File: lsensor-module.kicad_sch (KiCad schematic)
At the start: 27 parts, among them CN4 XHP-2, CN5 B2B-XH-A, Q4 BC847, U6 LMV358ID

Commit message: Назначение посадочных мест схемы
Дорисовка недостающий э/компонентов и важных 3D-моделей
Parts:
- R19: footprint lib:TRIM_PTN10-A01HB20 -> lib:Potentiometer_Bochen_PT10
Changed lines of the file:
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@@
 			)
 		)
-		(property "Footprint" "lib:TRIM_PTN10-A01HB20"
+		(property "Footprint" "lib:Potentiometer_Bochen_PT10"
 			(at 73.66 77.47 0)
 			(effects

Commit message: Разводка ПП, трассировка, оптимизация
Отказ от идеи с субмодулем, все разводится на двухсторонней ПП.
Вынос аналогового фотореле на отдельный лист схемы.
Разводка двусторонней ПП
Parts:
- R19: footprint lib:Potentiometer_Bochen_PT10 -> lib:TRIM_PTN10-A01HB20; Part Number PTN10-A200SB20 -> PTN10-A200HB20
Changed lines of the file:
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@@
 			)
 		)
-		(property "Footprint" "lib:Potentiometer_Bochen_PT10"
+		(property "Footprint" "lib:TRIM_PTN10-A01HB20"
 			(at 73.66 77.47 0)
 			(effects
@@
 			)
 		)
-		(property "Part Number" " PTN10-A200SB20"
+		(property "Part Number" "PTN10-A200HB20"
 			(at 76.962 88.392 90)
 			(effects

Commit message: Доделка ПП до финала
Проверка DRC, подгонка автоправил трассирования дорожек. Корректировка технических ограничений ПП. Расчет номиналов конденсаторов C11, C12.
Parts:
- renumbered C16 to C14, C17 to C15, C18 to C16, C19 to C17, C20 to C18, C21 to C19, C22 to C20, C23 to C21
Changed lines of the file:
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@@
 		(on_board yes)
 		(dnp no)
-		(property "Reference" "C22"
+		(property "Reference" "C20"
 			(at 162.56 76.2 0)
 			(effects
@@
 			(project "Camping-LightRelay"
 				(path "/5869d0d8-0214-47f7-a5b8-c2b5f6821b5d/65ad4b19-8f8d-472a-8529-1f5862972991"
-					(reference "C22")
+					(reference "C20")
 					(unit 1)
 				)
@@
 		(dnp no)
 		(fields_autoplaced yes)
-		(property "Reference" "#PWR028"
+		(property "Reference" "#PWR027"
 			(at 162.56 116.84 0)
 			(effects
@@
 			(project "Camping-LightRelay"
 				(path "/5869d0d8-0214-47f7-a5b8-c2b5f6821b5d/65ad4b19-8f8d-472a-8529-1f5862972991"
-					(reference "#PWR028")
+					(reference "#PWR027")
 					(unit 1)
 				)
@@
 		(on_board yes)
 		(dnp no)
-		(property "Reference" "C18"
+		(property "Reference" "C16"
 			(at 116.332 56.134 90)
 			(effects
@@
 			(project "Camping-LightRelay"
 				(path "/5869d0d8-0214-47f7-a5b8-c2b5f6821b5d/65ad4b19-8f8d-472a-8529-1f5862972991"
-					(reference "C18")
+					(reference "C16")
 					(unit 1)
 				)
@@
 		(dnp no)
 		(fields_autoplaced yes)
-		(property "Reference" "#PWR021"
+		(property "Reference" "#PWR020"
 			(at 73.66 116.84 0)
 			(effects
@@
 			(project "Camping-LightRelay"
 				(path "/5869d0d8-0214-47f7-a5b8-c2b5f6821b5d/65ad4b19-8f8d-472a-8529-1f5862972991"
-					(reference "#PWR021")
+					(reference "#PWR020")
 					(unit 1)
 				)
@@
 		(dnp no)
 		(fields_autoplaced yes)
-		(property "Reference" "#PWR025"
+		(property "Reference" "#PWR024"
 			(at 109.22 116.84 0)
 			(effects
@@
 			(project "Camping-LightRelay"
 				(path "/5869d0d8-0214-47f7-a5b8-c2b5f6821b5d/65ad4b19-8f8d-472a-8529-1f5862972991"
-					(reference "#PWR025")
+					(reference "#PWR024")
 					(unit 1)
 				)
@@
 		(on_board yes)
 		(dnp no)
-		(property "Reference" "C21"
+		(property "Reference" "C19"
 			(at 152.146 87.63 0)
 			(effects
@@
 			(project "Camping-LightRelay"
 				(path "/5869d0d8-0214-47f7-a5b8-c2b5f6821b5d/65ad4b19-8f8d-472a-8529-1f5862972991"
-					(reference "C21")
+					(reference "C19")
 					(unit 1)
 				)
@@
 		(dnp no)
 		(fields_autoplaced yes)
-		(property "Reference" "#PWR029"
+		(property "Reference" "#PWR028"
 			(at 170.18 116.84 0)
 			(effects
@@
 			(project "Camping-LightRelay"
 				(path "/5869d0d8-0214-47f7-a5b8-c2b5f6821b5d/65ad4b19-8f8d-472a-8529-1f5862972991"
-					(reference "#PWR029")
+					(reference "#PWR028")
 					(unit 1)
 				)
@@
 		(on_board yes)
 		(dnp no)
-		(property "Reference" "C19"
+		(property "Reference" "C17"
 			(at 130.81 65.278 0)
 			(effects
@@
 			(project "Camping-LightRelay"
 				(path "/5869d0d8-0214-47f7-a5b8-c2b5f6821b5d/65ad4b19-8f8d-472a-8529-1f5862972991"
-					(reference "C19")
+					(reference "C17")
 					(unit 1)
 				)
@@
 		(on_board yes)
 		(dnp no)
-		(property "Reference" "C16"
+		(property "Reference" "C14"
 			(at 90.17 70.866 0)
 			(effects
@@
 			(project "Camping-LightRelay"
 				(path "/5869d0d8-0214-47f7-a5b8-c2b5f6821b5d/65ad4b19-8f8d-472a-8529-1f5862972991"
-					(reference "C16")
+					(reference "C14")
 					(unit 1)
 				)
@@
 		(on_board yes)
 		(dnp no)
-		(property "Reference" "C23"
+		(property "Reference" "C21"
 			(at 191.77 90.678 90)
 			(effects
@@
 			(project "Camping-LightRelay"
 				(path "/5869d0d8-0214-47f7-a5b8-c2b5f6821b5d/65ad4b19-8f8d-472a-8529-1f5862972991"
-					(reference "C23")
+					(reference "C21")
 					(unit 1)
 				)
@@
 		(dnp no)
 		(fields_autoplaced yes)
-		(property "Reference" "#PWR023"
+		(property "Reference" "#PWR022"
 			(at 96.52 116.84 0)
 			(effects
@@
 			(project "Camping-LightRelay"
 				(path "/5869d0d8-0214-47f7-a5b8-c2b5f6821b5d/65ad4b19-8f8d-472a-8529-1f5862972991"
-					(reference "#PWR023")
+					(reference "#PWR022")
 					(unit 1)
 				)
@@
 		(dnp no)
 		(fields_autoplaced yes)
-		(property "Reference" "#PWR026"
+		(property "Reference" "#PWR025"
 			(at 138.43 116.84 0)
 			(effects
@@
 			(project "Camping-LightRelay"
 				(path "/5869d0d8-0214-47f7-a5b8-c2b5f6821b5d/65ad4b19-8f8d-472a-8529-1f5862972991"
-					(reference "#PWR026")
+					(reference "#PWR025")
 					(unit 1)
 				)
@@
 		(dnp no)
 		(fields_autoplaced yes)
-		(property "Reference" "#PWR031"
+		(property "Reference" "#PWR030"
 			(at 209.55 69.85 0)
 			(effects
@@
 			(project "Camping-LightRelay"
 				(path "/5869d0d8-0214-47f7-a5b8-c2b5f6821b5d/65ad4b19-8f8d-472a-8529-1f5862972991"
-					(reference "#PWR031")
+					(reference "#PWR030")
 					(unit 1)
 				)
@@
 		(dnp no)
 		(fields_autoplaced yes)
-		(property "Reference" "#PWR022"
+		(property "Reference" "#PWR021"
 			(at 90.17 116.84 0)
 			(effects
@@
 			(project "Camping-LightRelay"
 				(path "/5869d0d8-0214-47f7-a5b8-c2b5f6821b5d/65ad4b19-8f8d-472a-8529-1f5862972991"
-					(reference "#PWR022")
+					(reference "#PWR021")
 					(unit 1)
 				)
@@
 		(dnp no)
 		(fields_autoplaced yes)
-		(property "Reference" "#PWR024"
+		(property "Reference" "#PWR023"
 			(at 102.87 116.84 0)
 			(effects
@@
 			(project "Camping-LightRelay"
 				(path "/5869d0d8-0214-47f7-a5b8-c2b5f6821b5d/65ad4b19-8f8d-472a-8529-1f5862972991"
-					(reference "#PWR024")
+					(reference "#PWR023")
 					(unit 1)
 				)
@@
 		(on_board yes)
 		(dnp no)
-		(property "Reference" "C20"
+		(property "Reference" "C18"
 			(at 139.954 69.85 0)
 			(effects
@@
 			(project "Camping-LightRelay"
 				(path "/5869d0d8-0214-47f7-a5b8-c2b5f6821b5d/65ad4b19-8f8d-472a-8529-1f5862972991"
-					(reference "C20")
+					(reference "C18")
 					(unit 1)
 				)
@@
 		(dnp no)
 		(fields_autoplaced yes)
-		(property "Reference" "#PWR027"
+		(property "Reference" "#PWR026"
 			(at 154.94 116.84 0)
 			(effects
@@
 			(project "Camping-LightRelay"
 				(path "/5869d0d8-0214-47f7-a5b8-c2b5f6821b5d/65ad4b19-8f8d-472a-8529-1f5862972991"
-					(reference "#PWR027")
+					(reference "#PWR026")
 					(unit 1)
 				)
@@
 		(dnp no)
 		(fields_autoplaced yes)
-		(property "Reference" "#PWR030"
+		(property "Reference" "#PWR029"
 			(at 177.8 116.84 0)
 			(effects
@@
 			(project "Camping-LightRelay"
 				(path "/5869d0d8-0214-47f7-a5b8-c2b5f6821b5d/65ad4b19-8f8d-472a-8529-1f5862972991"
-					(reference "#PWR030")
+					(reference "#PWR029")
 					(unit 1)
 				)
@@
 		(on_board yes)
 		(dnp no)
-		(property "Reference" "C17"
+		(property "Reference" "C15"
 			(at 95.504 90.17 0)
 			(effects
@@
 			(project "Camping-LightRelay"
 				(path "/5869d0d8-0214-47f7-a5b8-c2b5f6821b5d/65ad4b19-8f8d-472a-8529-1f5862972991"
-					(reference "C17")
-					(unit 1)
-				)
+					(reference "C15")
+					(unit 1)
+				)

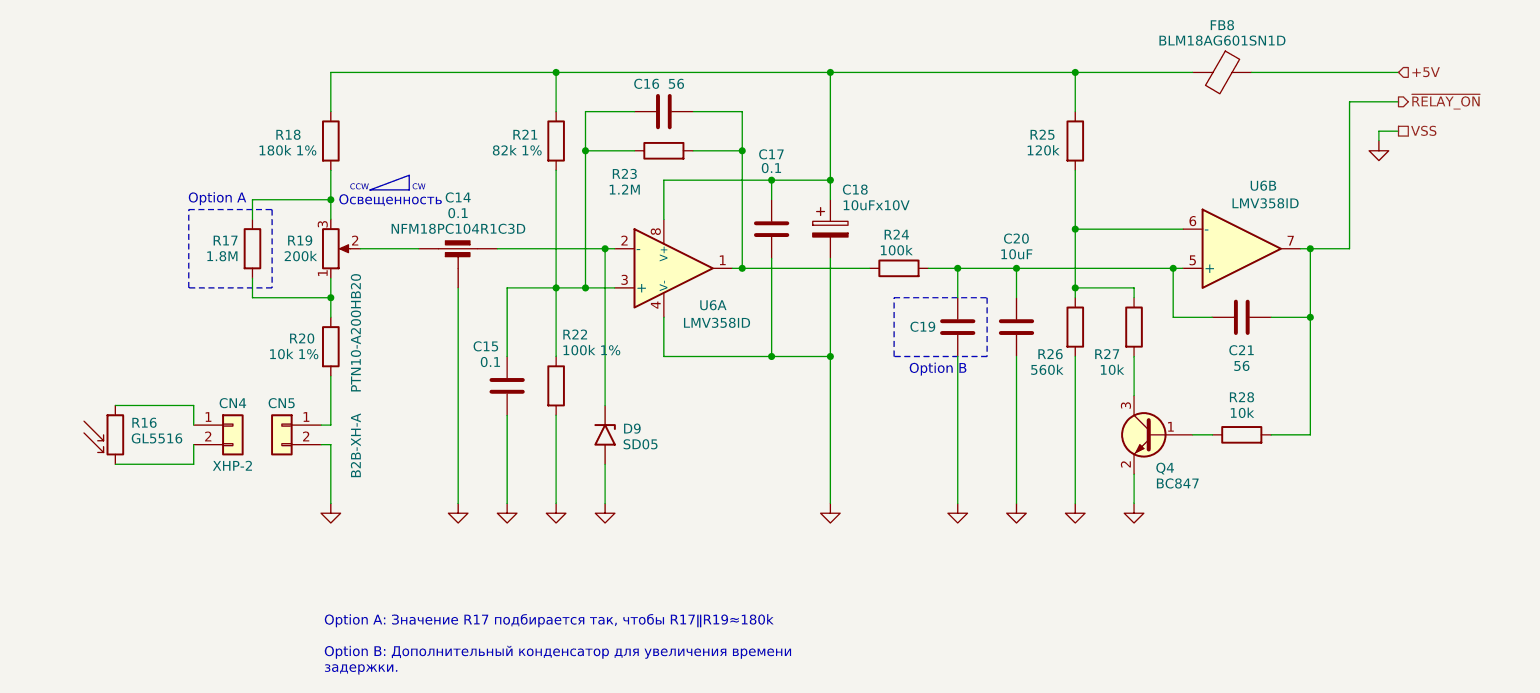
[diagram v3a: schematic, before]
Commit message: Первая сборка production
Сборка всей конструкции и проверка на ПП, проверка работы
* Правка посадочного места ионистор C3 и печатной платы для него
* Замена D3 на обычный 1N4148 из-за утечек Шоттки
* Замена стабилитрона D4 на двойной TVS-диод, т.к. обнаружился обходной ток от внутреннего DC/DC преобразователя
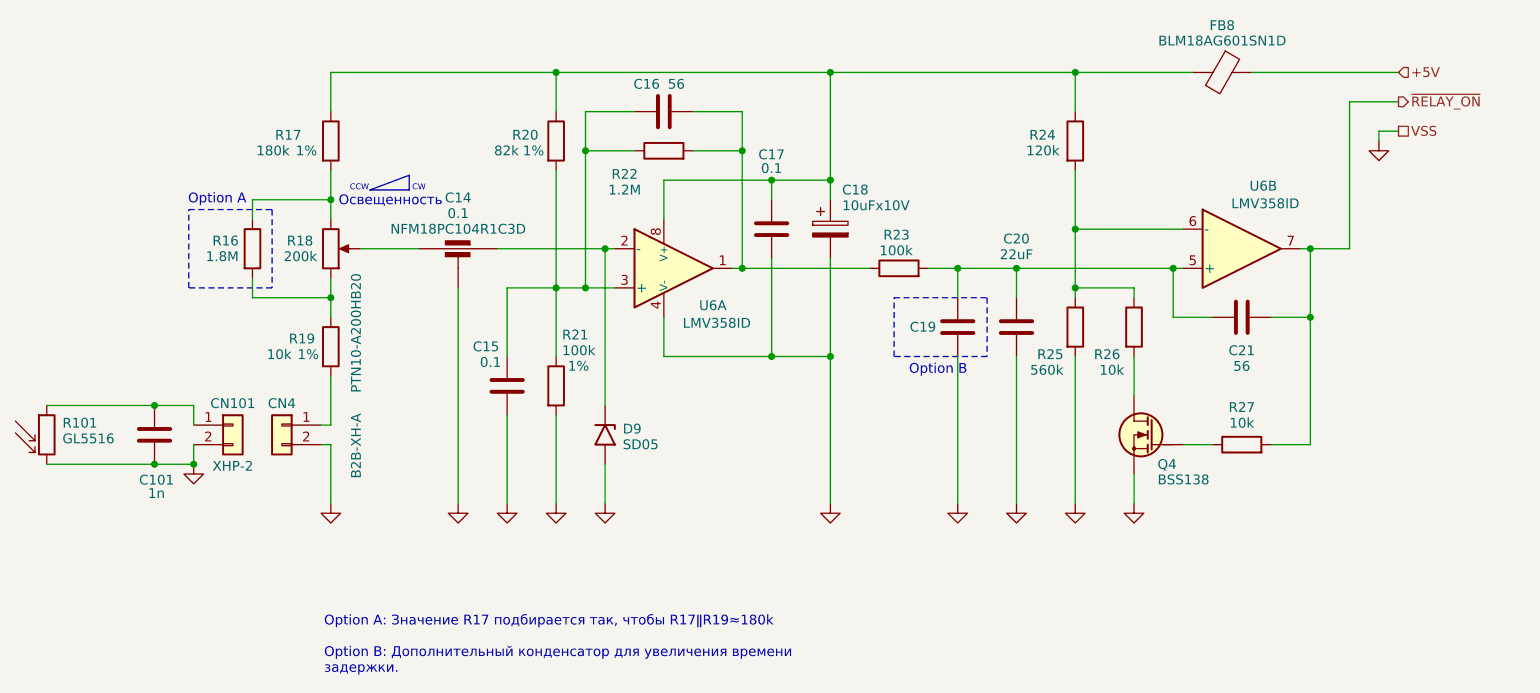
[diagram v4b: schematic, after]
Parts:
- removed Q4: BC847, Package_TO_SOT_SMD:SOT-23, symbol PCM_Transistor_BJT_AKL:BC847
- added C101: 1n, Capacitor_SMD:C_0603_1608Metric, symbol Device:C
- added Q4: BSS138, Package_TO_SOT_SMD:SOT-23, symbol PCM_Transistor_MOSFET_AKL:BSS138
- C20: value 10uF -> 22uF
- CN101: renamed from CN4; footprint (none) -> lib:PinSolder_1x2_P2.54mm; now left out of the parts list
- R17: renamed from R18; value 180k 1% -> 180k; Tolerance (none) -> 1%
- R19: renamed from R20; value 10k 1% -> 10k; Tolerance (none) -> 1%
- R20: renamed from R21; value 82k 1% -> 82k; Tolerance (none) -> 1%
- R21: renamed from R22; value 100k 1% -> 100k; Tolerance (none) -> 1%
- renumbered CN5 to CN4, R16 to R101, R17 to R16, R19 to R18, R23 to R22, R24 to R23, R25 to R24, R26 to R25, R27 to R26, R28 to R27
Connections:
- net GND: now also Q4.2 (S)
- net at R26.2: now also Q4.3 (D)
- net at R27.1: now also Q4.1 (G)
- net at CN101.1 (Pin_1), R101.1: now also C101.1
- net GND2: now reaches CN101.2 (Pin_2), R101.2
- net GND2: now also C101.2
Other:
- moved on the sheet: R101, R27

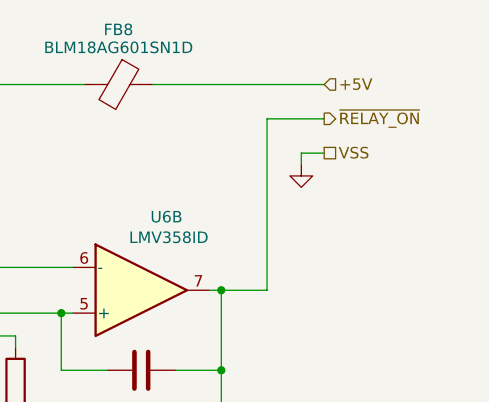
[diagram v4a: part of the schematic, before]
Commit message: Мелкий рефакторинг
- Обновление Readme.md
- Правки в печатную плату
- Переименование сигналов
- добавление исключений в .gitignore
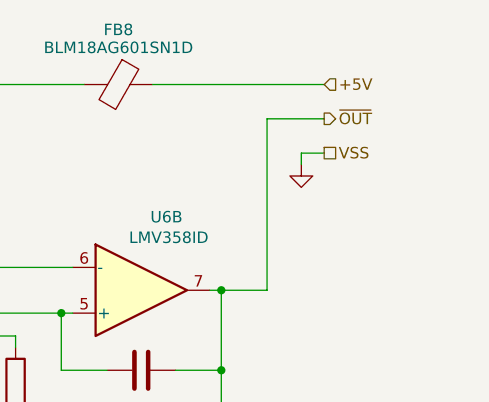
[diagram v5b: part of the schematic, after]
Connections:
- net ~{RELAY_ON} renamed ~{OUT}
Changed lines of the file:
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@@
 		)
 	)
-	(hierarchical_label "~{RELAY_ON}"
+	(hierarchical_label "~{OUT}"
 		(shape output)
 		(at 212.09 58.42 0)

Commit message: Обновление перед публикацией
- Удаление лишнего файла симуляции
- Рефакторинг электрической схемы и печатной платой.
- Добавление файла симуляции разряда ионистора.
- Удаление лишних захламляющих файлов
- Рефакторинг симуляции схем
- Обновление описания Readme
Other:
- title: (none) -> Субмодуля аналогового фотореле. Схема ЭП.
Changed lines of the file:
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@@
 	(paper "A4")
 	(title_block
+		(title "Субмодуля аналогового фотореле. Схема ЭП.")
 		(date "2024-05-12")
+		(rev "1.3")
+		(comment 1 "ФРК.42126.002-03 Э3")
 		(comment 2 "В.Иншаков")
+		(comment 7 "Э04.01.01 Э3")
 	)
 	(junction
